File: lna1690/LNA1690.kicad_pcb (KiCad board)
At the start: 2 copper layers, 75 x 45 mm, 38 parts, among them J1 Screw_Terminal_01x02, J2 Conn_Coaxial, J3 Conn_Coaxial, U1 TQP3M9008, U2 AMS1117-5.0, U3 TA1125A, U4 TQP3M9008, U5 TA1125A, U6 TQP3M9008

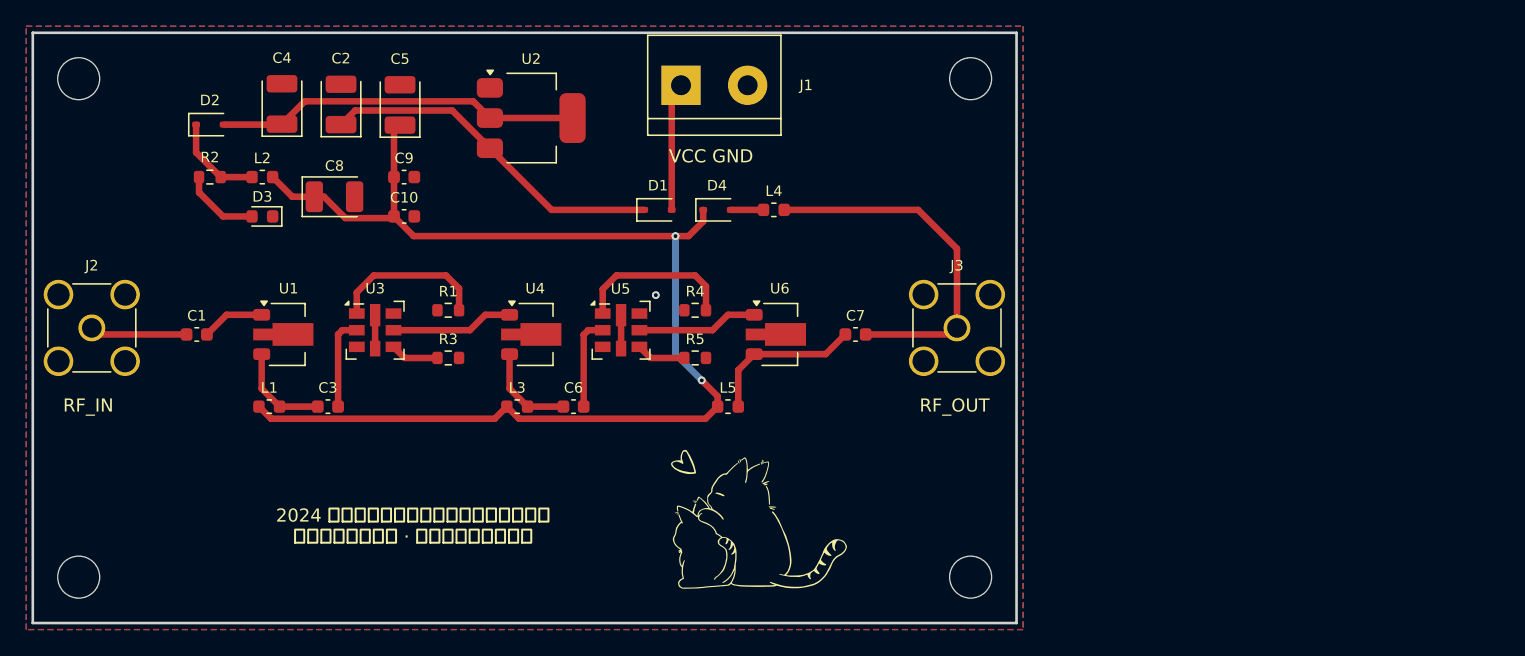
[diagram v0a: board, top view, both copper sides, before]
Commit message: Update LNA schematic
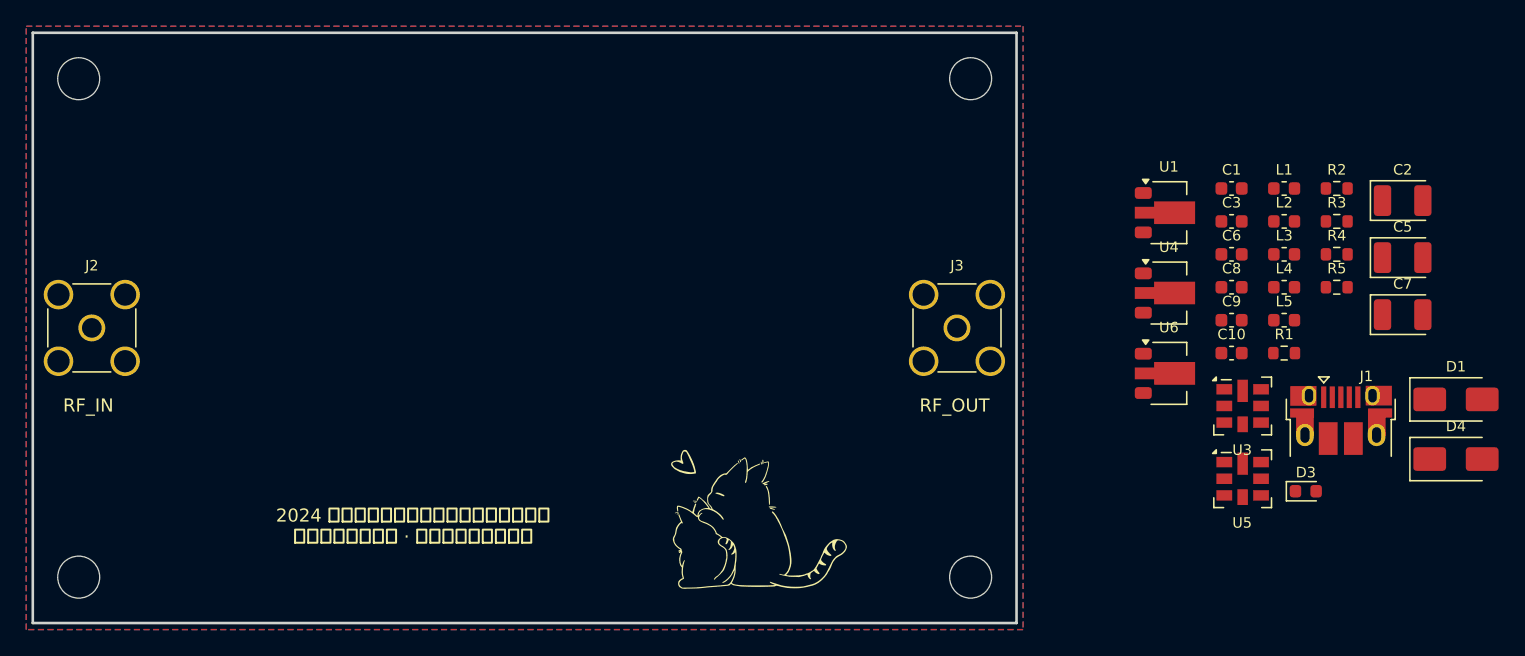
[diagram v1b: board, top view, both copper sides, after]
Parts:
- removed C4: 22uF, Capacitor_Tantalum_SMD:CP_EIA-3528-12_Kemet-T
- removed D2: 1N5819WS, Diode_SMD:D_SOD-323
- removed U2: AMS1117-5.0, Package_TO_SOT_SMD:SOT-223-3_TabPin2
- C10: value 0.1uF -> 22pF
- C7: value 22pF -> 10uF; footprint Capacitor_SMD:C_0603_1608Metric -> Capacitor_Tantalum_SMD:CP_EIA-3528-12_Kemet-T
- C8: value 10uF -> 0.1uF; footprint Capacitor_Tantalum_SMD:CP_EIA-3528-12_Kemet-T -> Capacitor_SMD:C_0603_1608Metric
- D1, D4: value 1N5819WS -> SS34; footprint Diode_SMD:D_SOD-323 -> Diode_SMD:D_SMA
- J1: value Screw_Terminal_01x02 -> USB_B_Micro; footprint TerminalBlock:TerminalBlock_bornier-2_P5.08mm -> Connector_USB:USB_Micro-B_Amphenol_10103594-0001LF_Horizontal
- L3: value 10uH -> 1uH
- moved R2 85.9 mm to (194.4, 71.9), turned to 0 degrees
- moved D3 82.3 mm to (192.1, 95.0), turned to 0 degrees
- moved C2 81.3 mm to (199.4, 72.8), turned to 0 degrees
- moved C1 79.7 mm to (186.4, 71.9)
- moved L1 79.1 mm to (190.4, 71.9)
- moved L2 78.0 mm to (190.4, 74.4)
- moved C5 77.3 mm to (199.4, 77.1), turned to 0 degrees
- moved C3 70.3 mm to (186.4, 74.4)
- moved C8 68.7 mm to (186.4, 79.4)
- moved R3 68.5 mm to (194.4, 74.4)
- moved U1 67.9 mm to (181.6, 73.7)
- moved U3 66.4 mm to (187.2, 88.5)
- moved C9 64.0 mm to (186.4, 81.9)
- moved C10 63.9 mm to (186.4, 84.4)
- moved R1 63.8 mm to (190.4, 84.4)
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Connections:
- C10 pad 1: +5V -> Net-(U6-OUT)
- C10 pad 2: GND -> /RF_OUT
- C7 pad 1: Net-(U6-OUT) -> +5V
- C7 pad 2: /RF_OUT -> GND
- J1 pad 2: GND -> unconnected-(J1-D--Pad2)
- L2 pad 1: Net-(D2-K) -> VCC
- R2 pad 1: Net-(D2-K) -> VCC
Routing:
- net +5V: track 94.1 -> 0.00 mm, vias 2 -> 0
- net Net-(D2-A): track 27.9 -> 0.00 mm
- net /RF_OUT: track 27.6 -> 0.00 mm
- net VCC: track 26.7 -> 0.00 mm
- net Net-(U5-INPUT_1): track 12.3 -> 0.00 mm
- net Net-(U6-OUT): track 12.1 -> 0.00 mm
- net Net-(U3-INPUT_1): track 12.0 -> 0.00 mm
- net Net-(D1-A): track 9.79 -> 0.00 mm
- net Net-(U3-OUTPUT_2): track 9.34 -> 0.00 mm
- net Net-(U5-OUTPUT_2): track 9.24 -> 0.00 mm
- net Net-(U1-OUT): track 7.47 -> 0.00 mm
- net Net-(J2-In): track 7.43 -> 0.00 mm
- net Net-(U4-OUT): track 7.30 -> 0.00 mm
- net Net-(D2-K): track 7.16 -> 0.00 mm
- net Net-(U5-INPUT_2): track 7.07 -> 0.00 mm
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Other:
- board text removed: "VCC GND"
